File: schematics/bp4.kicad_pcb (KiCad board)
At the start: 2 copper layers, 90 x 32.6 mm, 39 parts, among them J1 Left Pin Strip, J2 Right Pin Strip, J3 I/O Pin Strip, J4 Power Pins A, J5 Power Pins B, J6 Power Pins C, SW1 Power Switch, U1 TPS61220DCK, U2 LM321

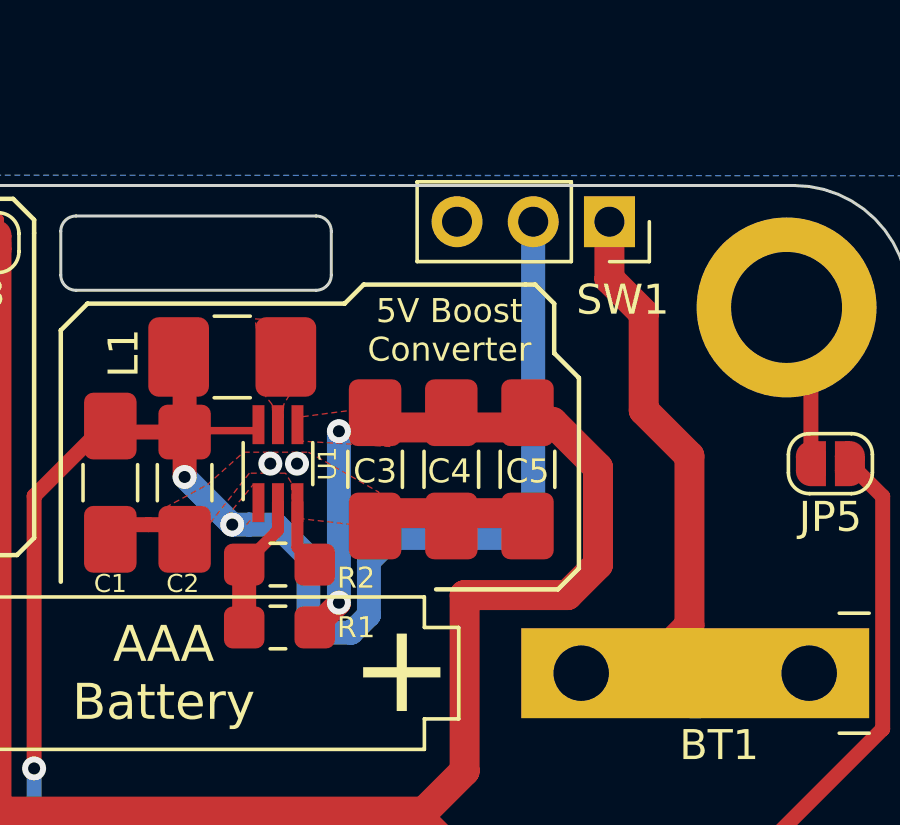
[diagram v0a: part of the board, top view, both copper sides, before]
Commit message: move SW1 to the left to make space for larger power switches
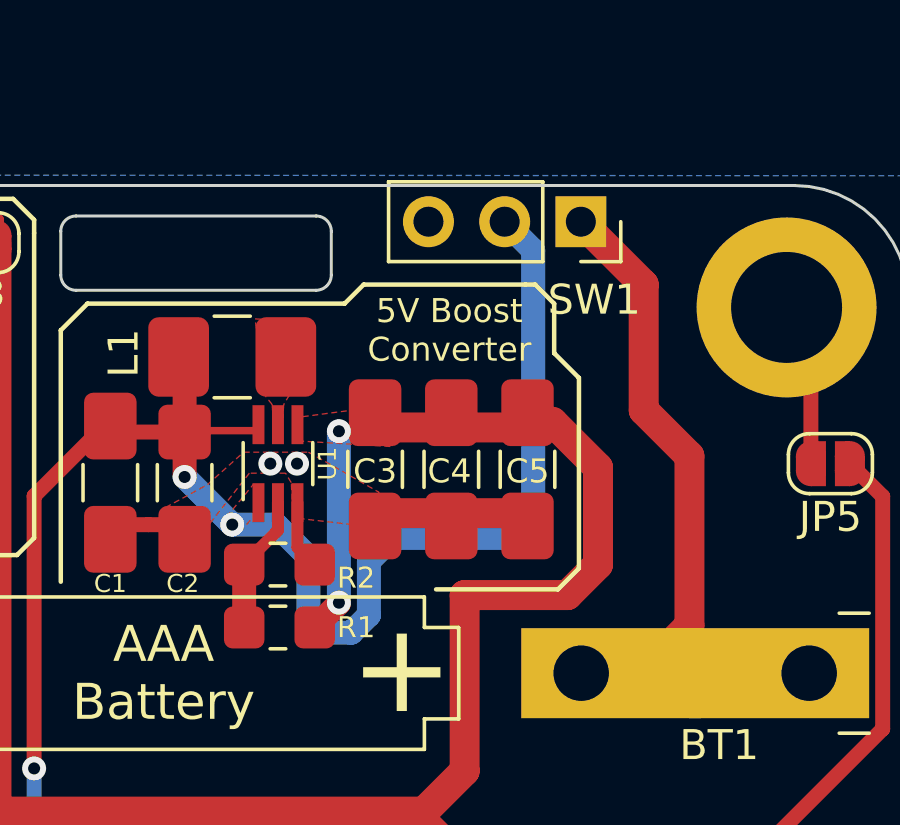
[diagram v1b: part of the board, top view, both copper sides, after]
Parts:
- moved SW1 0.95 mm to (104.5, 26.6)
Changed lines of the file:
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@@
     (thickness 1.6)
     (drawings 91)
-    (tracks 301)
+    (tracks 300)
     (zones 0)
     (modules 39)
@@
   )
   (setup
-    (last_trace_width 0.25)
+    (last_trace_width 1)
     (user_trace_width 0.4)
     (user_trace_width 0.5)
@@
   )
   (module Connector_PinSocket_2.54mm:PinSocket_1x03_P2.54mm_Vertical (layer F.Cu)
-    (at 105.41 26.6065 270)
+    (at 104.4575 26.6065 270)
     (descr "Through hole straight socket strip, 1x03, 2.54mm pitch, single row (from Kicad 4.0.7), script generated")
     (tags "Through hole socket strip THT 1x03 2.54mm single row")
@@
   (segment (start 74.4885 32.001) (end 73.2155 32.001) (width 1) (layer F.Cu) (net 1))
   (segment (start 104.469 41.656) (end 112.069 41.656) (width 0.4) (layer F.Cu) (net 2))
-  (segment (start 105.41 28.52) (end 106.553 29.663) (width 1) (layer F.Cu) (net 2))
-  (segment (start 105.41 26.67) (end 105.41 28.52) (width 1) (layer F.Cu) (net 2))
-  (segment (start 106.553 29.663) (end 106.553 32.893) (width 1) (layer F.Cu) (net 2))
+  (segment (start 108.077 40.0685) (end 106.4895 41.656) (width 1) (layer F.Cu) (net 2))
+  (segment (start 106.4895 41.656) (end 104.469 41.656) (width 1) (layer F.Cu) (net 2))
+  (segment (start 108.077 34.417) (end 108.077 40.0685) (width 1) (layer F.Cu) (net 2))
   (segment (start 106.553 32.893) (end 108.077 34.417) (width 1) (layer F.Cu) (net 2))
-  (segment (start 108.077 34.417) (end 108.077 40.0685) (width 1) (layer F.Cu) (net 2))
-  (segment (start 106.4895 41.656) (end 104.469 41.656) (width 1) (layer F.Cu) (net 2))
-  (segment (start 108.077 40.0685) (end 106.4895 41.656) (width 1) (layer F.Cu) (net 2))
+  (segment (start 106.553 28.702) (end 106.553 32.893) (width 1) (layer F.Cu) (net 2))
+  (segment (start 104.4575 26.6065) (end 106.553 28.702) (width 1) (layer F.Cu) (net 2))
   (segment (start 91.5845 33.571) (end 91.2495 33.906) (width 0.25) (layer F.Cu) (net 3))
   (segment (start 93.711 33.571) (end 91.5845 33.571) (width 0.25) (layer F.Cu) (net 3))
@@
   (segment (start 92.837 36.703) (end 92.837 36.645) (width 0.5) (layer F.Cu) (net 3))
   (segment (start 92.837 36.703) (end 91.2495 35.1155) (width 0.8) (layer B.Cu) (net 3))
-  (segment (start 93.402685 36.703) (end 92.837 36.703) (width 0.8) (layer B.Cu) (net 3))
-  (segment (start 95.377 37.7825) (end 94.2975 36.703) (width 0.8) (layer B.Cu) (net 3))
-  (segment (start 95.377 39.704727) (end 95.377 37.7825) (width 0.8) (layer B.Cu) (net 3))
-  (segment (start 95.978783 40.30651) (end 95.377 39.704727) (width 0.8) (layer B.Cu) (net 3))
-  (segment (start 97.39301 39.720717) (end 96.807217 40.30651) (width 0.8) (layer B.Cu) (net 3))
-  (segment (start 98.171 37.1475) (end 97.39301 37.92549) (width 0.8) (layer B.Cu) (net 3))
-  (segment (start 97.39301 37.92549) (end 97.39301 39.720717) (width 0.8) (layer B.Cu) (net 3))
-  (segment (start 102.1715 37.1475) (end 98.171 37.1475) (width 0.8) (layer B.Cu) (net 3))
-  (segment (start 94.2975 36.703) (end 93.402685 36.703) (width 0.8) (layer B.Cu) (net 3))
-  (segment (start 102.87 36.449) (end 102.1715 37.1475) (width 0.8) (layer B.Cu) (net 3))
-  (segment (start 96.807217 40.30651) (end 95.978783 40.30651) (width 0.8) (layer B.Cu) (net 3))
-  (segment (start 102.87 26.67) (end 102.87 36.449) (width 0.8) (layer B.Cu) (net 3))
   (segment (start 91.2495 35.1155) (end 91.2495 33.6185) (width 0.8) (layer F.Cu) (net 3))
+  (segment (start 102.87 27.559) (end 101.9175 26.6065) (width 0.8) (layer B.Cu) (net 3))
+  (segment (start 102.1715 37.1475) (end 102.87 36.449) (width 0.8) (layer B.Cu) (net 3))
+  (segment (start 98.171 37.1475) (end 102.1715 37.1475) (width 0.8) (layer B.Cu) (net 3))
+  (segment (start 97.39301 37.92549) (end 98.171 37.1475) (width 0.8) (layer B.Cu) (net 3))
+  (segment (start 97.39301 39.720717) (end 97.39301 37.92549) (width 0.8) (layer B.Cu) (net 3))
+  (segment (start 96.807217 40.30651) (end 97.39301 39.720717) (width 0.8) (layer B.Cu) (net 3))
+  (segment (start 95.978783 40.30651) (end 96.807217 40.30651) (width 0.8) (layer B.Cu) (net 3))
+  (segment (start 102.87 36.449) (end 102.87 27.559) (width 0.8) (layer B.Cu) (net 3))
+  (segment (start 95.377 39.704727) (end 95.978783 40.30651) (width 0.8) (layer B.Cu) (net 3))
+  (segment (start 94.2975 36.703) (end 95.377 37.7825) (width 0.8) (layer B.Cu) (net 3))
+  (segment (start 95.377 37.7825) (end 95.377 39.704727) (width 0.8) (layer B.Cu) (net 3))
+  (segment (start 92.837 36.703) (end 94.2975 36.703) (width 0.8) (layer B.Cu) (net 3))
   (segment (start 29.337 49.276) (end 29.21 49.276) (width 1) (layer F.Cu) (net 4))
   (segment (start 97.6025 33.4615) (end 97.5995 33.4645) (width 0.5) (layer F.Cu) (net 4))

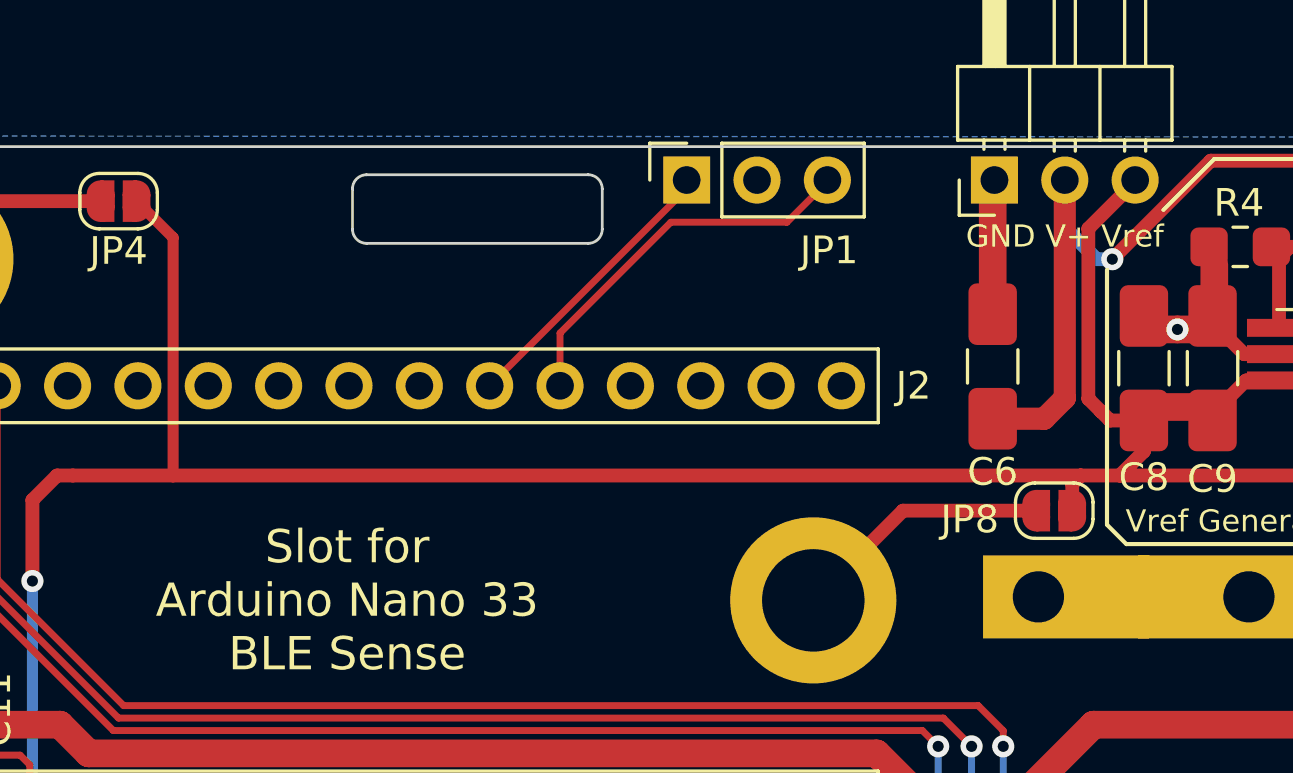
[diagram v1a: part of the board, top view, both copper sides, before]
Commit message: move JP8 away from battery clip to avoid short circuit with ground
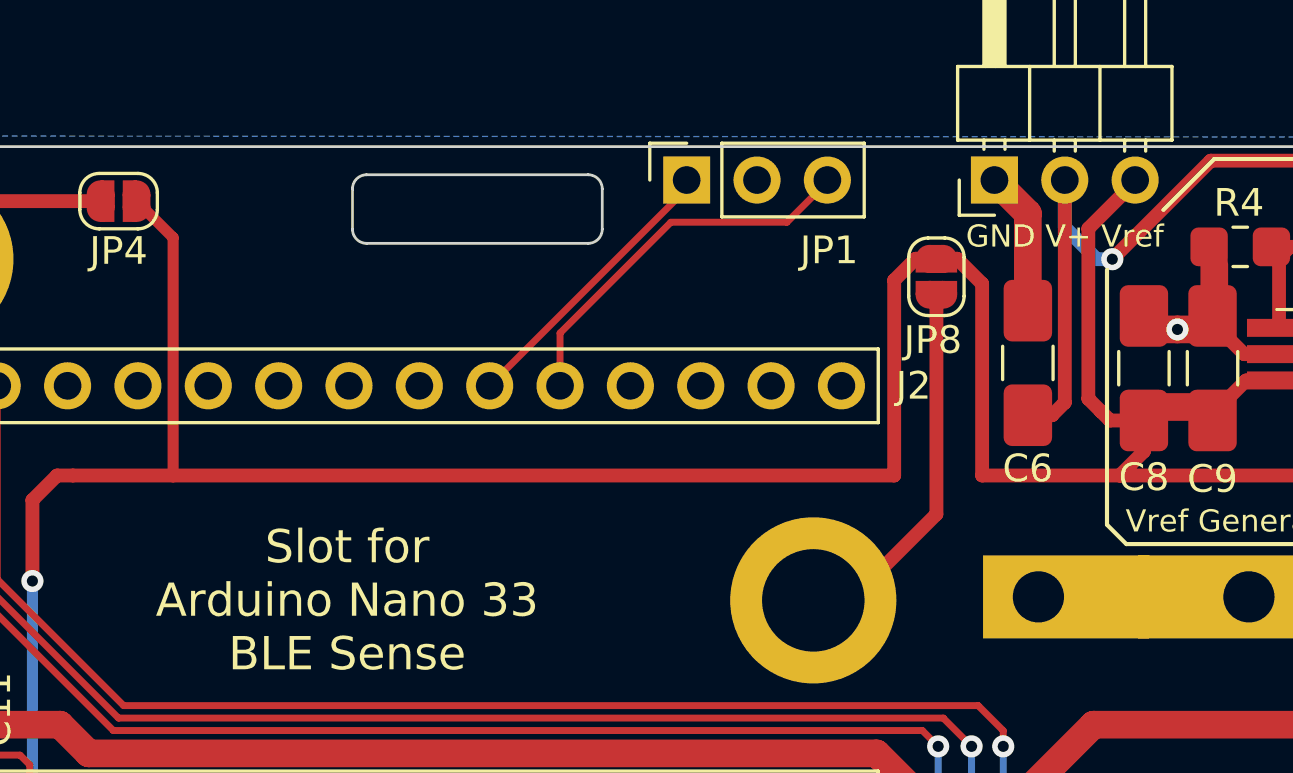
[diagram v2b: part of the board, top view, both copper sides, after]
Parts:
- moved JP8 9.46 mm to (65.8, 30.1), turned to 270 degrees
- moved C6 1.28 mm to (69.1, 33.2)
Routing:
- net /Vref: track 171.5 -> 184.8 mm
- net Net-(JP8-Pad2): track 9.39 -> 13.7 mm
- net /V+: track 180.1 -> 178.9 mm
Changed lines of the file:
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@@
     (thickness 1.6)
     (drawings 91)
-    (tracks 300)
+    (tracks 306)
     (zones 0)
     (modules 39)
@@
   )
   (setup
-    (last_trace_width 1)
+    (last_trace_width 0.5)
     (user_trace_width 0.4)
     (user_trace_width 0.5)
@@
   )
   (module Capacitor_SMD:C_1206_3216Metric_Pad1.42x1.75mm_HandSolder (layer F.Cu)
-    (at 67.818 33.3375 90)
+    (at 69.088 33.2105 90)
     (descr "Capacitor SMD 1206 (3216 Metric), square (rectangular) end terminal, IPC_7351 nominal with elongated pad for handsoldering. (Body size source: http://www.tortai-tech.com/upload/download/2011102023233369053.pdf), generated with kicad-footprint-generator")
     (tags "capacitor handsolder")
@@
       (effects (font (size 1 1) (thickness 0.15)))
     )
-    (fp_line (start -1.6 0.8) (end -1.6 -0.8) (layer F.Fab) (width 0.1))
-    (fp_line (start -1.6 -0.8) (end 1.6 -0.8) (layer F.Fab) (width 0.1))
-    (fp_line (start 1.6 -0.8) (end 1.6 0.8) (layer F.Fab) (width 0.1))
-    (fp_line (start 1.6 0.8) (end -1.6 0.8) (layer F.Fab) (width 0.1))
-    (fp_line (start -0.602064 -0.91) (end 0.602064 -0.91) (layer F.SilkS) (width 0.12))
-    (fp_line (start -0.602064 0.91) (end 0.602064 0.91) (layer F.SilkS) (width 0.12))
-    (fp_line (start -2.45 1.12) (end -2.45 -1.12) (layer F.CrtYd) (width 0.05))
-    (fp_line (start -2.45 -1.12) (end 2.45 -1.12) (layer F.CrtYd) (width 0.05))
-    (fp_line (start 2.45 -1.12) (end 2.45 1.12) (layer F.CrtYd) (width 0.05))
-    (fp_line (start 2.45 1.12) (end -2.45 1.12) (layer F.CrtYd) (width 0.05))
     (fp_text user %R (at 0 0 90) (layer F.Fab)
       (effects (font (size 0.8 0.8) (thickness 0.12)))
     )
+    (fp_line (start 2.45 1.12) (end -2.45 1.12) (layer F.CrtYd) (width 0.05))
+    (fp_line (start 2.45 -1.12) (end 2.45 1.12) (layer F.CrtYd) (width 0.05))
+    (fp_line (start -2.45 -1.12) (end 2.45 -1.12) (layer F.CrtYd) (width 0.05))
+    (fp_line (start -2.45 1.12) (end -2.45 -1.12) (layer F.CrtYd) (width 0.05))
+    (fp_line (start -0.602064 0.91) (end 0.602064 0.91) (layer F.SilkS) (width 0.12))
+    (fp_line (start -0.602064 -0.91) (end 0.602064 -0.91) (layer F.SilkS) (width 0.12))
+    (fp_line (start 1.6 0.8) (end -1.6 0.8) (layer F.Fab) (width 0.1))
+    (fp_line (start 1.6 -0.8) (end 1.6 0.8) (layer F.Fab) (width 0.1))
+    (fp_line (start -1.6 -0.8) (end 1.6 -0.8) (layer F.Fab) (width 0.1))
+    (fp_line (start -1.6 0.8) (end -1.6 -0.8) (layer F.Fab) (width 0.1))
+    (pad 2 smd roundrect (at 1.8875 0 90) (size 2.225 1.75) (layers F.Cu F.Paste F.Mask) (roundrect_rratio 0.175)
+      (net 1 /GND))
     (pad 1 smd roundrect (at -1.8875 0 90) (size 2.225 1.75) (layers F.Cu F.Paste F.Mask) (roundrect_rratio 0.175)
       (net 4 /V+))
-    (pad 2 smd roundrect (at 1.8875 0 90) (size 2.225 1.75) (layers F.Cu F.Paste F.Mask) (roundrect_rratio 0.175)
-      (net 1 /GND))
     (model ${KISYS3DMOD}/Capacitor_SMD.3dshapes/C_1206_3216Metric.wrl
       (at (xyz 0 0 0))
@@
   )
   (module Jumper:SolderJumper-2_P1.3mm_Open_RoundedPad1.0x1.5mm (layer F.Cu)
-    (at 70.0405 38.5445 180)
+    (at 65.786 30.099 270)
     (descr "SMD Solder Jumper, 1x1.5mm, rounded Pads, 0.3mm gap, open")
     (tags "solder jumper open")
     (attr virtual)
-    (fp_text reference JP8 (at 3.048 -0.3175) (layer F.SilkS)
-      (effects (font (size 1 1) (thickness 0.15)))
-    )
-    (fp_text value SolderJumper_2_Open (at 0 1.9) (layer F.Fab)
+    (fp_text reference JP8 (at 2.286 0.127 180) (layer F.SilkS)
+      (effects (font (size 1 1) (thickness 0.15)))
+    )
+    (fp_text value SolderJumper_2_Open (at 0 1.9 90) (layer F.Fab)
       (effects (font (size 1 1) (thickness 0.15)))
     )
@@
     (fp_arc (start 0.7 0.3) (end 0.7 1) (angle -90) (layer F.SilkS) (width 0.12))
     (fp_arc (start 0.7 -0.3) (end 1.4 -0.3) (angle -90) (layer F.SilkS) (width 0.12))
-    (pad 2 smd custom (at 0.65 0 180) (size 1 0.5) (layers F.Cu F.Mask)
+    (pad 2 smd custom (at 0.65 0 270) (size 1 0.5) (layers F.Cu F.Mask)
       (net 42 "Net-(JP8-Pad2)") (zone_connect 2)
       (options (clearance outline) (anchor rect))
@@
            (xy 0 -0.75) (xy -0.5 -0.75) (xy -0.5 0.75) (xy 0 0.75)) (width 0))
       ))
-    (pad 1 smd custom (at -0.65 0 180) (size 1 0.5) (layers F.Cu F.Mask)
+    (pad 1 smd custom (at -0.65 0 270) (size 1 0.5) (layers F.Cu F.Mask)
       (net 6 /Vref) (zone_connect 2)
       (options (clearance outline) (anchor rect))
@@
   (segment (start 75.819 32.001) (end 74.4885 32.001) (width 1) (layer F.Cu) (net 1))
   (segment (start 67.818 26.7335) (end 67.8815 26.67) (width 1) (layer F.Cu) (net 1))
-  (segment (start 67.818 32.001) (end 67.818 26.7335) (width 1) (layer F.Cu) (net 1))
   (segment (start 88.773 36.706) (end 90.04 36.706) (width 0.5) (layer F.Cu) (net 1))
   (segment (start 102.5495 36.2645) (end 102.5525 36.2615) (width 0.5) (layer F.Cu) (net 1))
@@
   (segment (start 99.7125 53.7845) (end 99.7125 55.961) (width 0.5) (layer F.Cu) (net 1))
   (segment (start 74.4885 32.001) (end 73.2155 32.001) (width 1) (layer F.Cu) (net 1))
+  (segment (start 69.088 27.813) (end 67.8815 26.6065) (width 1) (layer F.Cu) (net 1))
+  (segment (start 69.088 31.323) (end 69.088 27.813) (width 1) (layer F.Cu) (net 1))
   (segment (start 104.469 41.656) (end 112.069 41.656) (width 0.4) (layer F.Cu) (net 2))
   (segment (start 108.077 40.0685) (end 106.4895 41.656) (width 1) (layer F.Cu) (net 2))
@@
   (segment (start 29.337 49.276) (end 29.21 49.276) (width 1) (layer F.Cu) (net 4))
   (segment (start 97.6025 33.4615) (end 97.5995 33.4645) (width 0.5) (layer F.Cu) (net 4))
-  (segment (start 67.818 35.225) (end 69.677 35.225) (width 0.8) (layer F.Cu) (net 4))
-  (segment (start 70.4215 34.4805) (end 70.4215 26.67) (width 0.8) (layer F.Cu) (net 4))
   (segment (start 100.584 39.0525) (end 104.013 39.0525) (width 1) (layer F.Cu) (net 4))
   (segment (start 104.013 39.0525) (end 105.029 38.0365) (width 1) (layer F.Cu) (net 4))
@@
   (segment (start 63.627 47.3075) (end 65.278 48.9585) (width 1) (layer F.Cu) (net 4))
   (segment (start 35.179 47.3075) (end 63.627 47.3075) (width 1) (layer F.Cu) (net 4))
-  (segment (start 69.677 35.225) (end 70.4215 34.4805) (width 0.8) (layer F.Cu) (net 4))
   (segment (start 100.665 44.997998) (end 100.584 44.916998) (width 0.5) (layer F.Cu) (net 4))
   (segment (start 99.229999 46.270999) (end 101.9635 49.0045) (width 0.5) (layer F.Cu) (net 4))
@@
   (segment (start 72.136 29.464) (end 71.570315 29.464) (width 0.5) (layer B.Cu) (net 4))
   (segment (start 70.4215 28.315185) (end 70.4215 26.67) (width 0.5) (layer B.Cu) (net 4))
+  (segment (start 69.963 35.098) (end 69.088 35.098) (width 0.5) (layer F.Cu) (net 4))
+  (segment (start 70.4215 34.6395) (end 69.963 35.098) (width 0.5) (layer F.Cu) (net 4))
+  (segment (start 70.4215 26.6065) (end 70.4215 34.6395) (width 0.5) (layer F.Cu) (net 4))
   (segment (start 82.608 31.943) (end 83.3755 31.1755) (width 0.5) (layer F.Cu) (net 5))
   (segment (start 80.856 31.943) (end 82.608 31.943) (width 0.5) (layer F.Cu) (net 5))
@@
   (segment (start 105.6005 52.19) (end 105.6005 56.769) (width 0.5) (layer F.Cu) (net 6))
   (segment (start 102.8135 49.403) (end 105.6005 52.19) (width 0.5) (layer F.Cu) (net 6))
-  (segment (start 70.6905 37.577) (end 70.6905 38.5445) (width 0.5) (layer F.Cu) (net 6))
-  (segment (start 70.993 37.2745) (end 70.6905 37.577) (width 0.5) (layer F.Cu) (net 6))
-  (segment (start 72.4055 37.2745) (end 70.993 37.2745) (width 0.5) (layer F.Cu) (net 6))
   (segment (start 38.227 28.687) (end 36.9085 27.3685) (width 0.4) (layer F.Cu) (net 6))
   (segment (start 38.227 37.2745) (end 38.227 28.687) (width 0.4) (layer F.Cu) (net 6))
-  (segment (start 70.993 37.2745) (end 38.227 37.2745) (width 0.5) (layer F.Cu) (net 6))
   (segment (start 38.227 37.2745) (end 34.6075 37.2745) (width 0.5) (layer F.Cu) (net 6))
   (segment (start 33.147 38.1635) (end 33.147 41.0845) (width 0.5) (layer F.Cu) (net 6))
@@
   (segment (start 105.4585 49.403) (end 105.5855 49.53) (width 0.5) (layer F.Cu) (net 6))
   (segment (start 102.8135 49.403) (end 105.4585 49.403) (width 0.5) (layer F.Cu) (net 6))
+  (segment (start 66.533592 29.449) (end 65.786 29.449) (width 0.5) (layer F.Cu) (net 6))
+  (segment (start 67.437 30.352408) (end 66.533592 29.449) (width 0.5) (layer F.Cu) (net 6))
+  (segment (start 67.437 37.2745) (end 67.437 30.352408) (width 0.5) (layer F.Cu) (net 6))
+  (segment (start 72.4055 37.2745) (end 67.437 37.2745) (width 0.5) (layer F.Cu) (net 6))
+  (segment (start 65.038408 29.449) (end 64.262 30.225408) (width 0.5) (layer F.Cu) (net 6))
+  (segment (start 65.786 29.449) (end 65.038408 29.449) (width 0.5) (layer F.Cu) (net 6))
+  (segment (start 64.262 30.225408) (end 64.262 37.2745) (width 0.5) (layer F.Cu) (net 6))
+  (segment (start 64.262 37.2745) (end 38.227 37.2745) (width 0.5) (layer F.Cu) (net 6))
   (segment (start 32.7025 47.371) (end 32.7025 47.371) (width 0.25) (layer F.Cu) (net 7))
   (via (at 30.876818 47.386818) (size 0.8) (drill 0.4) (layers F.Cu B.Cu) (net 7))
@@
   (segment (start 111.267 53.9115) (end 111.3155 53.9115) (width 0.5) (layer F.Cu) (net 41))
   (segment (start 106.8855 49.53) (end 111.267 53.9115) (width 0.5) (layer F.Cu) (net 41))
-  (segment (start 64.5795 38.5445) (end 61.341 41.783) (width 0.5) (layer F.Cu) (net 42))
-  (segment (start 69.3905 38.5445) (end 64.5795 38.5445) (width 0.5) (layer F.Cu) (net 42))
+  (segment (start 61.341 41.783) (end 62.6745 41.783) (width 0.5) (layer F.Cu) (net 42))
+  (segment (start 65.786 38.6715) (end 65.786 30.749) (width 0.5) (layer F.Cu) (net 42))
+  (segment (start 62.6745 41.783) (end 65.786 38.6715) (width 0.5) (layer F.Cu) (net 42))
   (zone (net 1) (net_name /GND) (layer B.Cu) (hatch edge 0.508)
     (connect_pads (clearance 0.508))
